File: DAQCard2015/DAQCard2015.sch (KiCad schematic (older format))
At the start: 0 parts

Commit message: Updates to DAQ Card including FPGA card pinout and completion of ADC Stage
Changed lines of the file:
@@
 $Descr A2 23386 16535
 encoding utf-8
-Sheet 1 3
+Sheet 1 13
 Title ""
 Date ""
@@
 $EndDescr
 $Sheet
-S 3400 2250 1900 650
+S 2150 2250 1650 11200
 U 55C47A4C
 F0 "Frontend" 60
 F1 "Frontend.sch" 60
+F2 "ADC_CLK+" I L 2150 2450 60
+F3 "ADC_CLK-" I L 2150 2550 60
+F4 "1D-D" O R 3800 2500 60
+F5 "1D+D" O R 3800 2600 60
+F6 "1D-C" O R 3800 2700 60
+F7 "1D+C" O R 3800 2800 60
+F8 "1D-B" O R 3800 2900 60
+F9 "1D+B" O R 3800 3000 60
+F10 "1D-A" O R 3800 3100 60
+F11 "1D+A" O R 3800 3200 60
+F12 "1FCO-" O R 3800 3350 60
+F13 "1FCO+" O R 3800 3450 60
+F14 "1DCO-" O R 3800 3550 60
+F15 "1DCO+" O R 3800 3650 60
+F16 "2D-D" O R 3800 3850 60
+F17 "2D+D" O R 3800 3950 60
+F18 "2D-C" O R 3800 4050 60
+F19 "2D+C" O R 3800 4150 60
+F20 "2D-B" O R 3800 4250 60
+F21 "2D+B" O R 3800 4350 60
+F22 "2D-A" O R 3800 4450 60
+F23 "2D+A" O R 3800 4550 60
+F24 "2FCO-" O R 3800 4700 60
+F25 "2FCO+" O R 3800 4800 60
+F26 "2DCO-" O R 3800 4900 60
+F27 "2DCO+" O R 3800 5000 60
+F28 "4D+D" O R 3800 6650 60
+F29 "4D-C" O R 3800 6750 60
+F30 "4D+C" O R 3800 6850 60
+F31 "4D-B" O R 3800 6950 60
+F32 "4D+B" O R 3800 7050 60
+F33 "4D-A" O R 3800 7150 60
+F34 "4D+A" O R 3800 7250 60
+F35 "4FCO-" O R 3800 7400 60
+F36 "4FCO+" O R 3800 7500 60
+F37 "4DCO-" O R 3800 7650 60
+F38 "4DCO+" O R 3800 7750 60
+F39 "3D-D" O R 3800 5200 60
+F40 "3D+D" O R 3800 5300 60
+F41 "3D-C" O R 3800 5400 60
+F42 "3D+C" O R 3800 5500 60
+F43 "3D-B" O R 3800 5600 60
+F44 "3D+B" O R 3800 5700 60
+F45 "3D-A" O R 3800 5800 60
+F46 "3D+A" O R 3800 5900 60
+F47 "3FCO-" O R 3800 6050 60
+F48 "3FCO+" O R 3800 6150 60
+F49 "3DCO-" O R 3800 6250 60
+F50 "3DCO+" O R 3800 6350 60
+F51 "ADC_SCLK" I L 2150 2900 60
+F52 "ADC_SDIO" I L 2150 3000 60
+F53 "1ADC_CSB" I L 2150 3100 60
+F54 "8D-D" O R 3800 12050 60
+F55 "8D+D" O R 3800 12150 60
+F56 "8D-C" O R 3800 12250 60
+F57 "8D+C" O R 3800 12350 60
+F58 "8D-B" O R 3800 12450 60
+F59 "8D+B" O R 3800 12550 60
+F60 "8D-A" O R 3800 12650 60
+F61 "8D+A" O R 3800 12750 60
+F62 "8FCO-" O R 3800 12900 60
+F63 "8FCO+" O R 3800 13000 60
+F64 "8DCO-" O R 3800 13100 60
+F65 "8DCO+" O R 3800 13200 60
+F66 "7D-D" O R 3800 10700 60
+F67 "7D+D" O R 3800 10800 60
+F68 "7D-C" O R 3800 10900 60
+F69 "7D+C" O R 3800 11000 60
+F70 "7D-B" O R 3800 11100 60
+F71 "7D+B" O R 3800 11200 60
+F72 "7D-A" O R 3800 11300 60
+F73 "7D+A" O R 3800 11400 60
+F74 "7FCO-" O R 3800 11550 60
+F75 "7FCO+" O R 3800 11650 60
+F76 "7DCO-" O R 3800 11750 60
+F77 "7DCO+" O R 3800 11850 60
+F78 "5D-D" O R 3800 7950 60
+F79 "5D+D" O R 3800 8050 60
+F80 "5D-C" O R 3800 8150 60
+F81 "5D+C" O R 3800 8250 60
+F82 "5D-B" O R 3800 8350 60
+F83 "5D+B" O R 3800 8450 60
+F84 "5D-A" O R 3800 8550 60
+F85 "5D+A" O R 3800 8650 60
+F86 "5FCO-" O R 3800 8800 60
+F87 "5FCO+" O R 3800 8900 60
+F88 "5DCO-" O R 3800 9050 60
+F89 "5DCO+" O R 3800 9150 60
+F90 "6D-D" O R 3800 9350 60
+F91 "6D+D" O R 3800 9450 60
+F92 "6D-C" O R 3800 9550 60
+F93 "6D+C" O R 3800 9650 60
+F94 "6D-B" O R 3800 9750 60
+F95 "6D+B" O R 3800 9850 60
+F96 "6D-A" O R 3800 9950 60
+F97 "6D+A" O R 3800 10050 60
+F98 "6FCO-" O R 3800 10200 60
+F99 "6FCO+" O R 3800 10300 60
+F100 "6DCO-" O R 3800 10400 60
+F101 "6DCO+" O R 3800 10500 60
+F102 "4D-D" O R 3800 6550 60
+F103 "2ADC_CSB" I L 2150 3200 60
+F104 "3ADC_CSB" I L 2150 3300 60
+F105 "4ADC_CSB" I L 2150 3400 60
+F106 "5ADC_CSB" I L 2150 3500 60
+F107 "6ADC_CSB" I L 2150 3600 60
+F108 "7ADC_CSB" I L 2150 3700 60
+F109 "8ADC_CSB" I L 2150 3800 60
+F110 "RNGDAC_CSB" I L 2150 3900 60
+$EndSheet
+$Sheet
+S 8000 1950 3150 13400
+U 55C86A60
+F0 "ZEM4310" 60
+F1 "ZEM4310.sch" 60
+$EndSheet
+$Sheet
+S 18200 1700 4100 2350
+U 55C9D43F
+F0 "MISCIO" 60
+F1 "MISCIO.sch" 60
+F2 "EXT_TRG" I L 18200 1950 60
+F3 "EXT_CLK" I L 18200 2050 60
+F4 "UIO_1" I L 18200 2150 60
+F5 "UIO_2" I L 18200 2250 60
+$EndSheet
+$Sheet
+S 17700 5250 4100 2750
+U 55D3B55F
+F0 "Power" 60
+F1 "Power.sch" 60
 $EndSheet
 $EndSCHEMATC

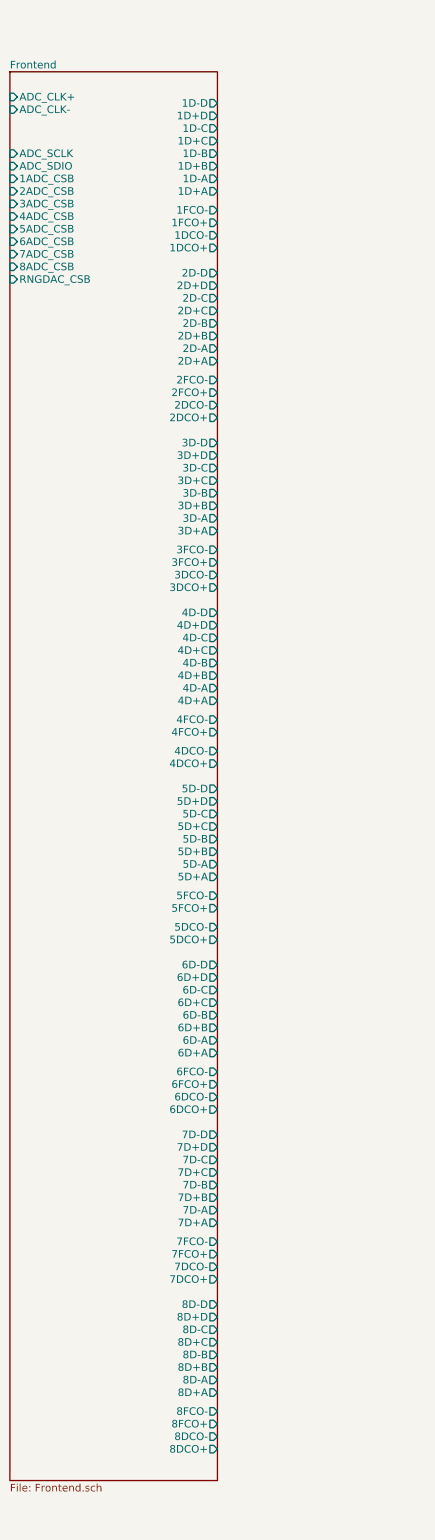
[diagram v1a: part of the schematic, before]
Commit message: Adds power circuitry to DAQCard2015
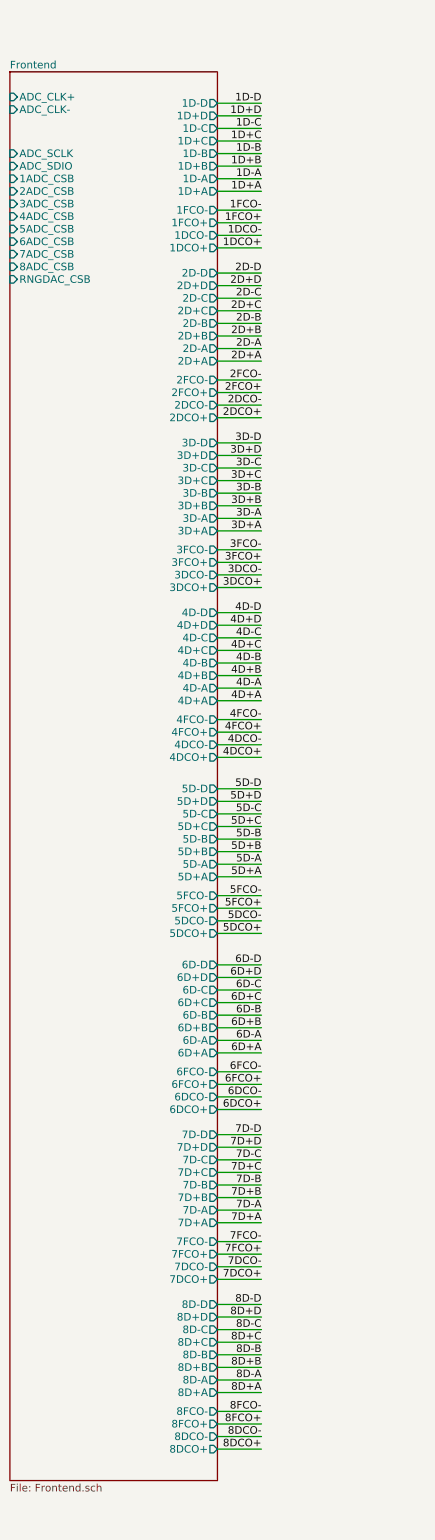
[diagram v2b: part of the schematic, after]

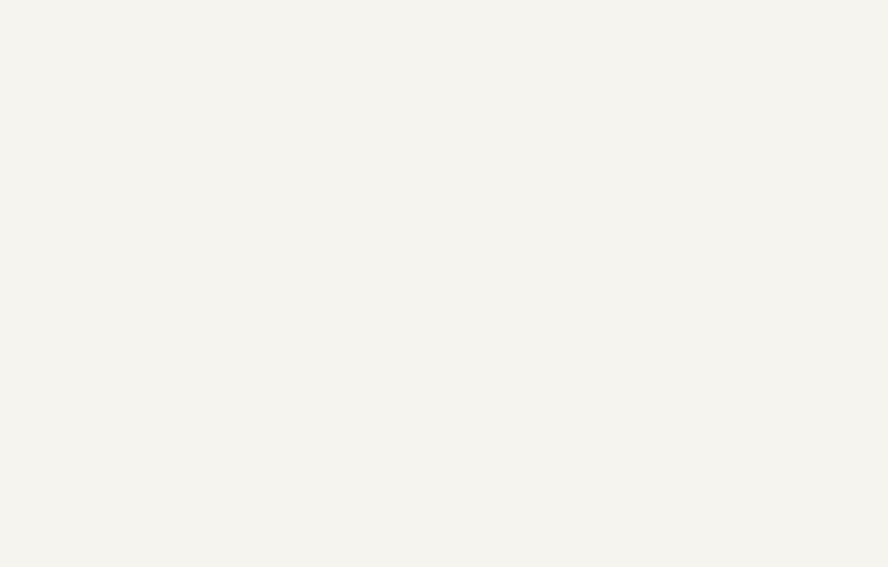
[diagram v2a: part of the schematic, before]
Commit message: Finishes initial version of schematic(mostly). And adds a whole bunch of new footprints!
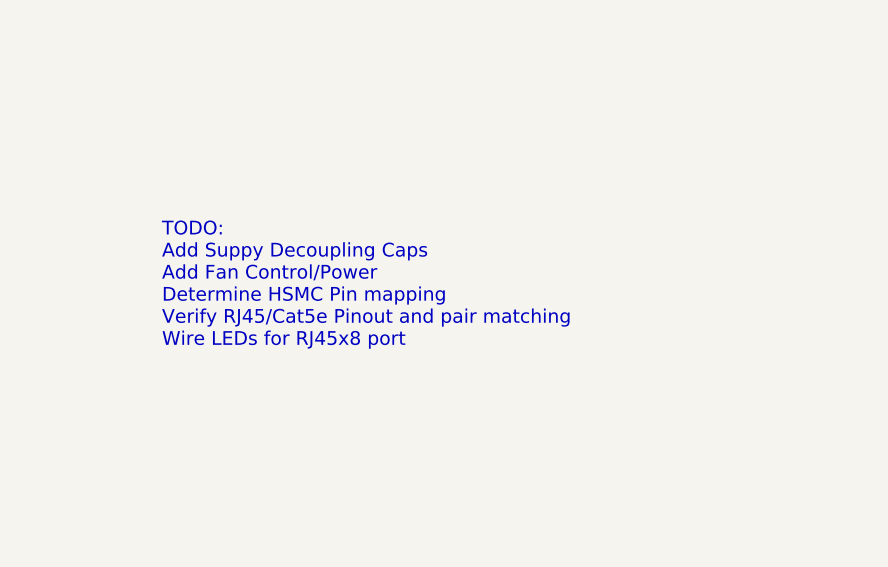
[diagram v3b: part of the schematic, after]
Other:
- note added: "TODO:\nAdd Suppy Decoupling Caps\nAdd Fan Control/Power\nDetermine HSMC Pin mapping\nVerify RJ45/Cat5e Pinout and pair matching\nWire LEDs for RJ45x8 port"
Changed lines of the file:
@@
 Text Label 4150 13200 2    60   ~ 0
 8DCO+
+Text Notes 14100 9250 0    60   ~ 0
+TODO:\nAdd Suppy Decoupling Caps\nAdd Fan Control/Power\nDetermine HSMC Pin mapping\nVerify RJ45/Cat5e Pinout and pair matching\nWire LEDs for RJ45x8 port
 $EndSCHEMATC

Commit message: Adds a more-or-less complete BOM to DAQ Card
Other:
- note added: "TODO:\nAdd Suppy Decoupling Caps\nAdd Fan Control/Power\nDetermine HSMC Pin mapping\nVerify RJ45/Cat5e Pinout and pair matching\nWire LEDs for RJ45x8 port\nAPC128 Control Lines w/ 2x20 Header"
- note removed: "TODO:\nAdd Suppy Decoupling Caps\nAdd Fan Control/Power\nDetermine HSMC Pin mapping\nVerify RJ45/Cat5e Pinout and pair matching\nWire LEDs for RJ45x8 port"
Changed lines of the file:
@@
 8DCO+
 Text Notes 14100 9250 0    60   ~ 0
-TODO:\nAdd Suppy Decoupling Caps\nAdd Fan Control/Power\nDetermine HSMC Pin mapping\nVerify RJ45/Cat5e Pinout and pair matching\nWire LEDs for RJ45x8 port
+TODO:\nAdd Suppy Decoupling Caps\nAdd Fan Control/Power\nDetermine HSMC Pin mapping\nVerify RJ45/Cat5e Pinout and pair matching\nWire LEDs for RJ45x8 port\nAPC128 Control Lines w/ 2x20 Header
 $EndSCHEMATC

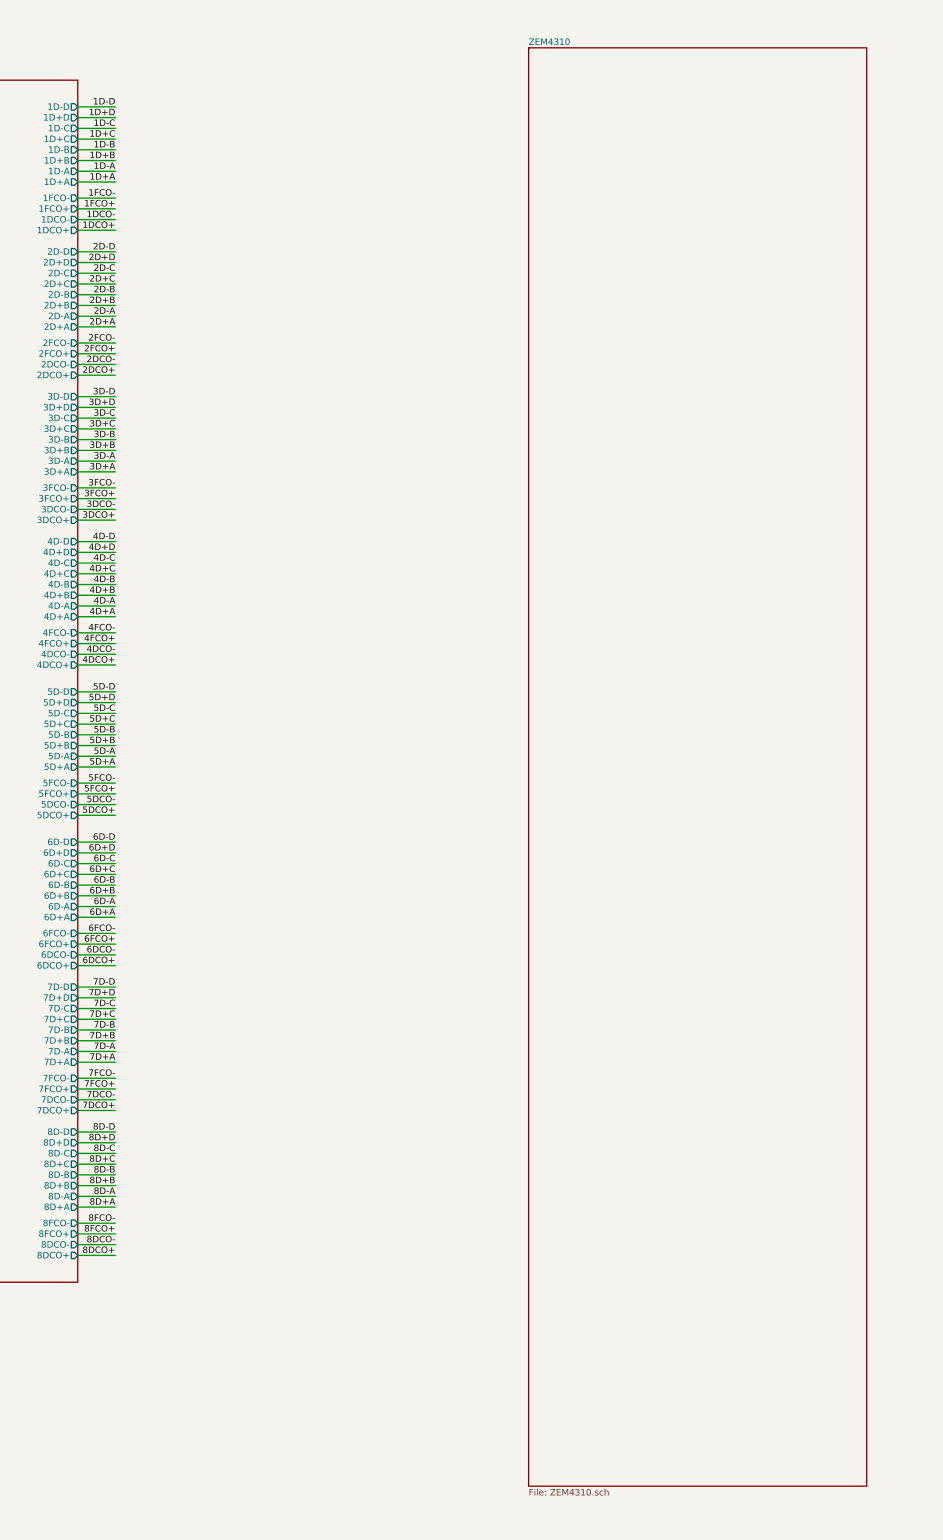
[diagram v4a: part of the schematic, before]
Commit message: LVDS pins assigned and first round routing finished, work on 3d models
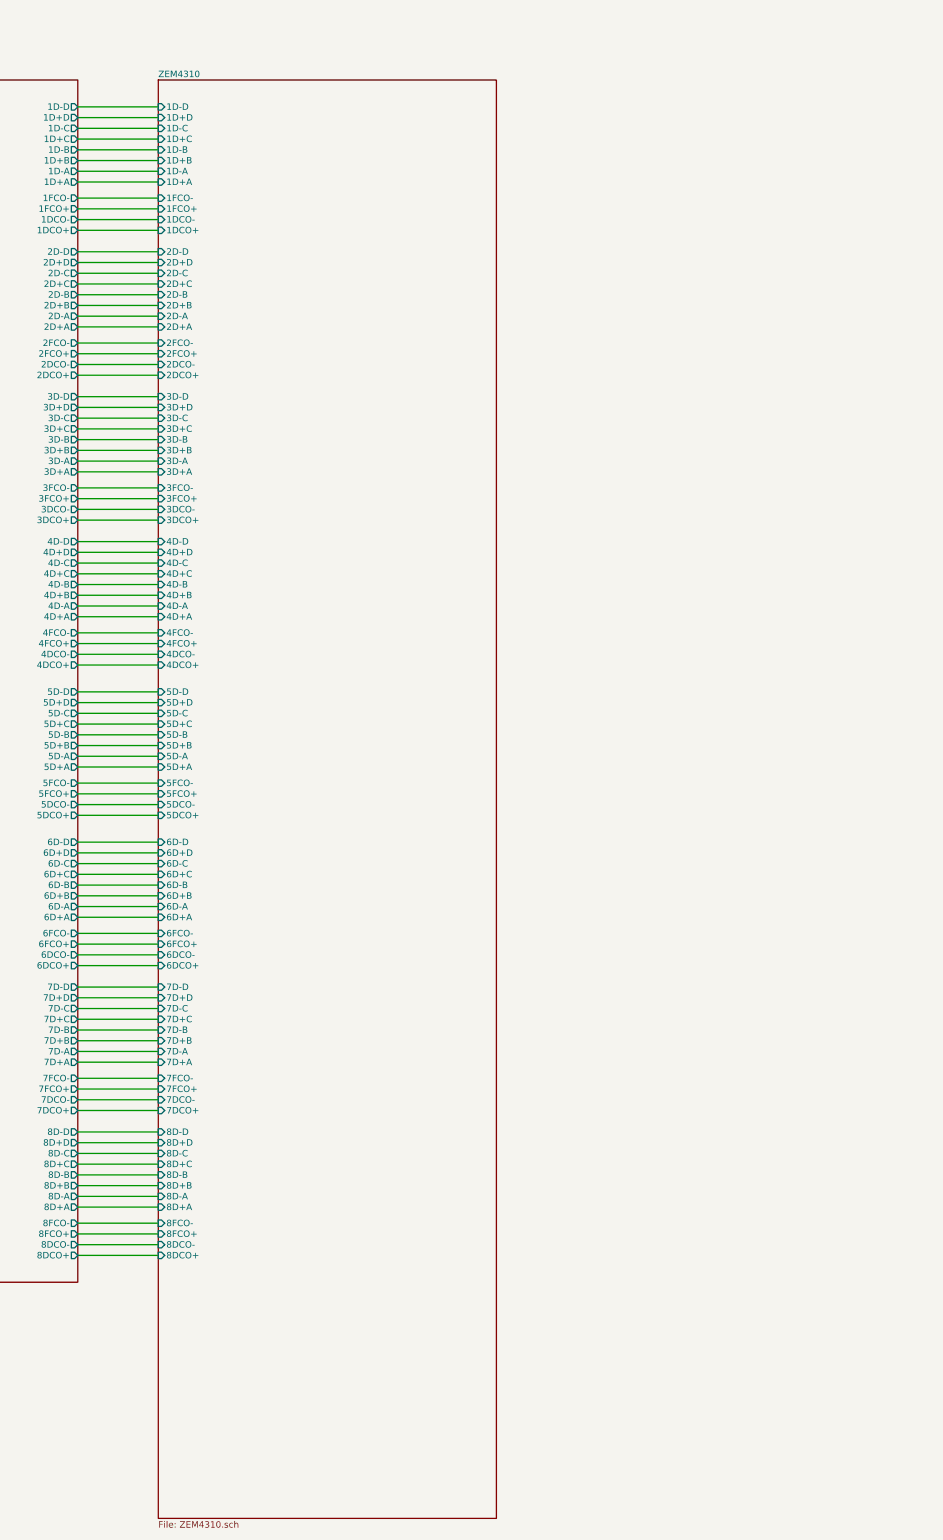
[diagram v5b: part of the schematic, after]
